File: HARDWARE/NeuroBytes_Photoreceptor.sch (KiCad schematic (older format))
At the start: 21 parts, among them P1 JST_GH_4-POS, P2 JST_GH_4-POS, P3 JST_GH_5-pos, SW1 SW_PB_4term, SW2 SW_PB_4term, U1 APDS9007, U2 STM32L011Gx, U3 3v3 LDO

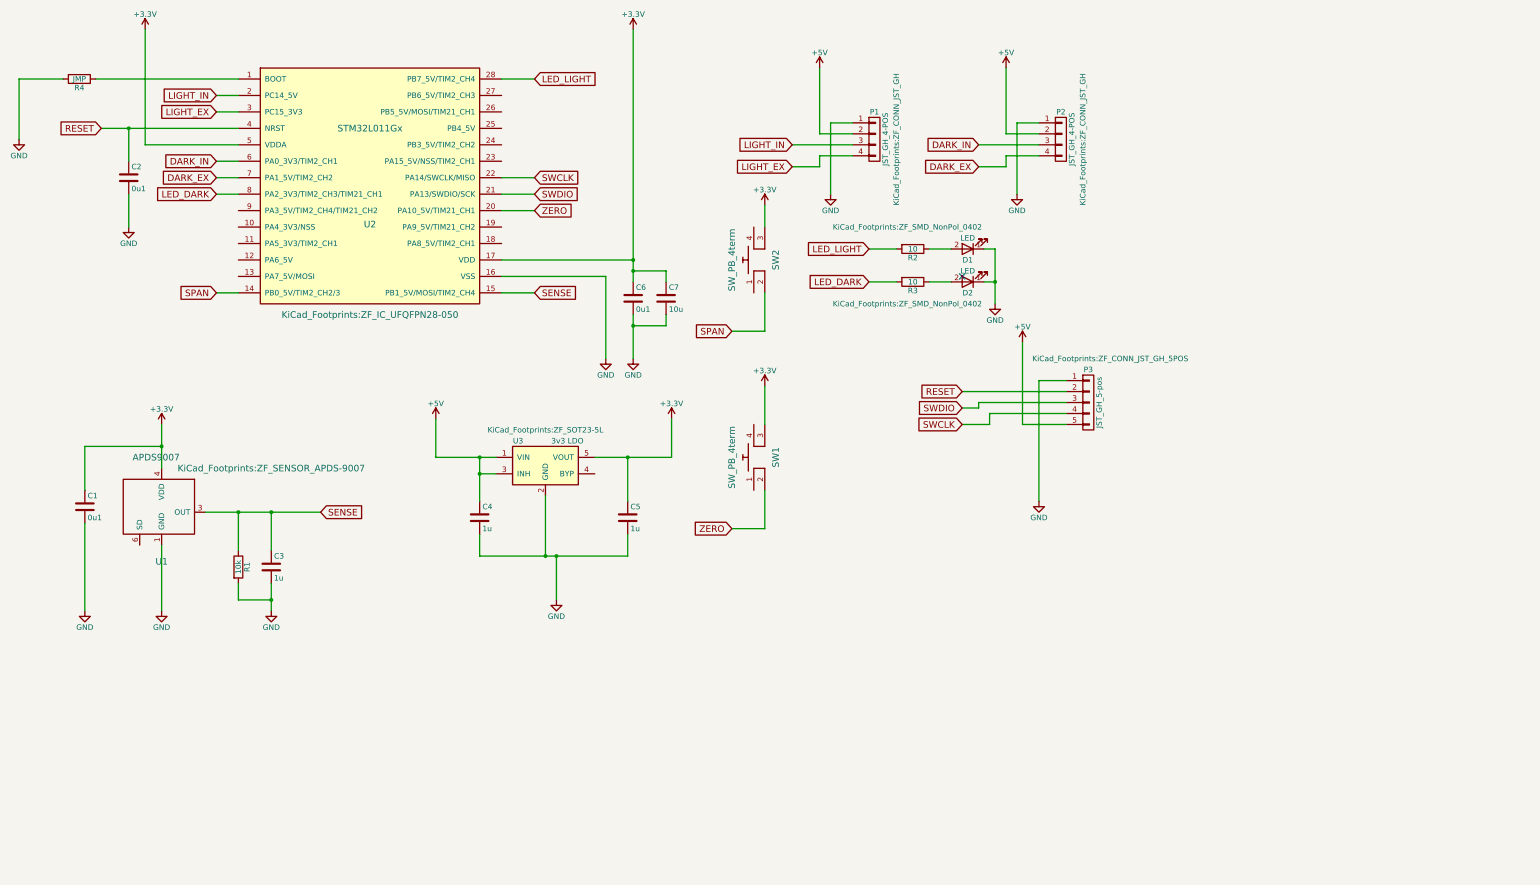
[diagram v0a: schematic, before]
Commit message: minor page layout updates
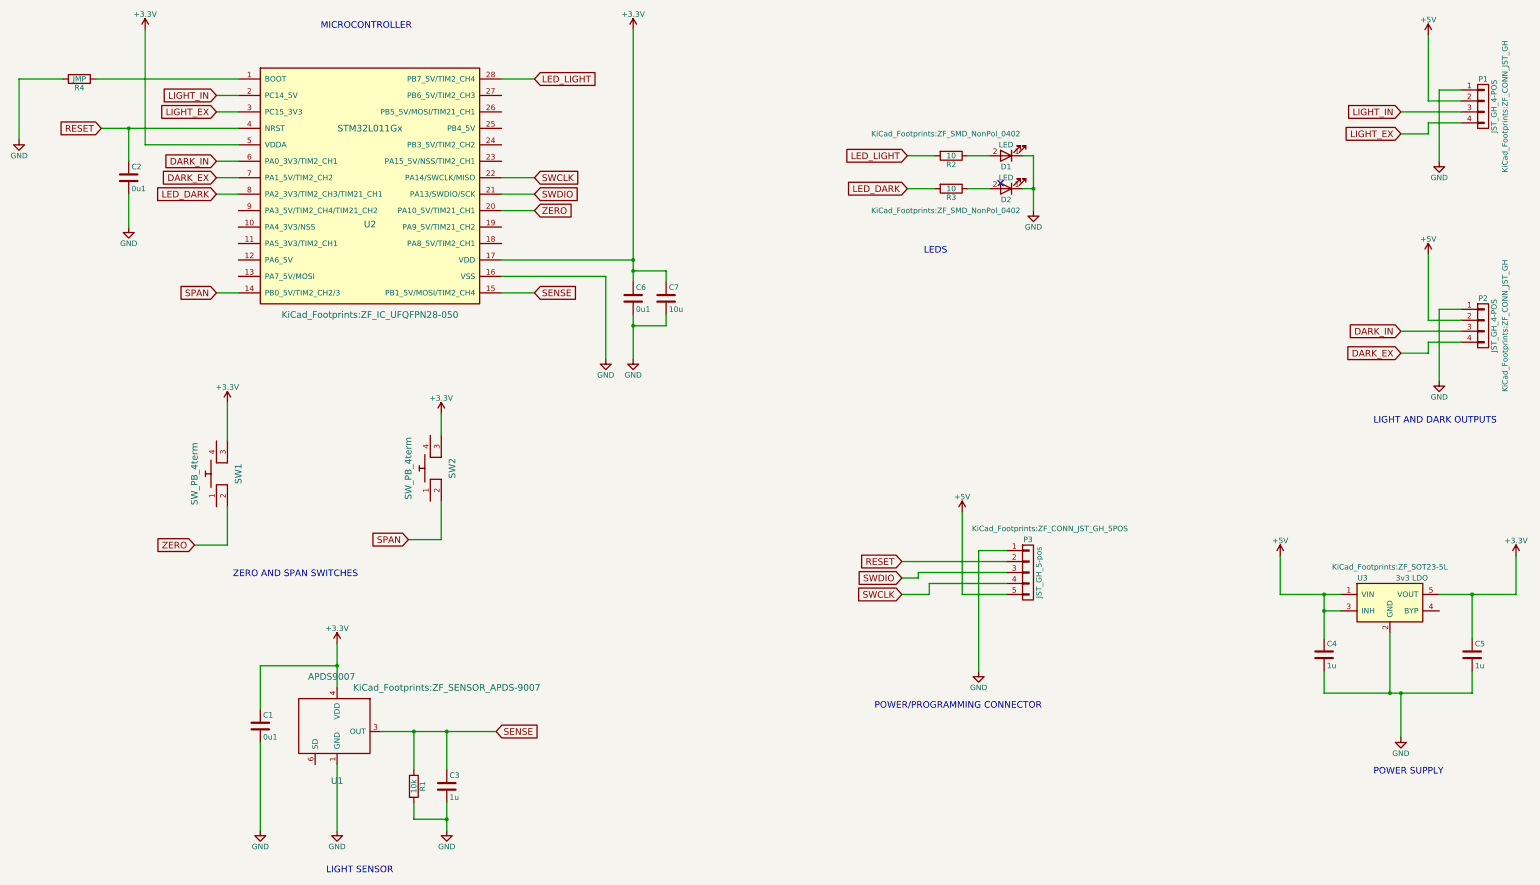
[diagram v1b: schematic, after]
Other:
- note added: "LEDS"
- note added: "LIGHT AND DARK OUTPUTS"
- note added: "LIGHT SENSOR"
- note added: "MICROCONTROLLER"
- note added: "POWER SUPPLY"
- note added: "POWER/PROGRAMMING CONNECTOR"
- note added: "ZERO AND SPAN SWITCHES"
- moved on the sheet: C1, C3, C4, C5, D1, D2, P1, P2, P3, R1, R2, R3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

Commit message: added ESD protection. updated title block. minor routing changes.
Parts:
- added U4: RClamp0503F, KiCad_Footprints:ZF_SMD_SOT-353, symbol RClamp0503F
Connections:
- net +3V3: now also U4.5 (VCC)
- net GND: now also U4.2 (GND)
- net SENSE: now also U4.1 (SIG1)
- net SPAN: now also U4.3 (SIG2)
- net ZERO: now also U4.4 (SIG3)
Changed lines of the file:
@@
 Rev "E"
 Comp "NeuroTinker LLC"
-Comment1 "License: GPL v3"
-Comment2 ""
+Comment1 "(C) 2018 Zach Fredin"
+Comment2 "License: CC-BY-SA 4.0"
 Comment3 ""
 Comment4 ""
@@
 $EndComp
 $Comp
-L +5V #PWR8
+L +5V #PWR01
 U 1 1 58B9AB7F
 P 12400 6100
-F 0 "#PWR8" H 12400 5950 50  0001 C CNN
+F 0 "#PWR01" H 12400 5950 50  0001 C CNN
 F 1 "+5V" H 12400 6240 50  0000 C CNN
 F 2 "" H 12400 6100 50  0000 C CNN
@@
 $EndComp
 $Comp
-L +3.3V #PWR13
+L +3.3V #PWR02
 U 1 1 58B9B0DC
 P 14550 6100
-F 0 "#PWR13" H 14550 5950 50  0001 C CNN
+F 0 "#PWR02" H 14550 5950 50  0001 C CNN
 F 1 "+3.3V" H 14550 6240 50  0000 C CNN
 F 2 "" H 14550 6100 50  0000 C CNN
@@
 $EndComp
 $Comp
-L GND #PWR9
+L GND #PWR03
 U 1 1 58B9B110
 P 13500 7750
-F 0 "#PWR9" H 13500 7500 50  0001 C CNN
+F 0 "#PWR03" H 13500 7500 50  0001 C CNN
 F 1 "GND" H 13500 7600 50  0000 C CNN
 F 2 "" H 13500 7750 50  0000 C CNN
@@
 $EndComp
 $Comp
-L +3.3V #PWR4
+L +3.3V #PWR04
 U 1 1 58B9B1C8
 P 2050 1300
-F 0 "#PWR4" H 2050 1150 50  0001 C CNN
+F 0 "#PWR04" H 2050 1150 50  0001 C CNN
 F 1 "+3.3V" H 2050 1440 50  0000 C CNN
 F 2 "" H 2050 1300 50  0000 C CNN
@@
 $EndComp
 $Comp
-L +3.3V #PWR11
+L +3.3V #PWR05
 U 1 1 58B9B218
 P 6500 1300
-F 0 "#PWR11" H 6500 1150 50  0001 C CNN
+F 0 "#PWR05" H 6500 1150 50  0001 C CNN
 F 1 "+3.3V" H 6500 1440 50  0000 C CNN
 F 2 "" H 6500 1300 50  0000 C CNN
@@
 $EndComp
 $Comp
-L GND #PWR10
+L GND #PWR06
 U 1 1 58B9B234
 P 6250 4300
-F 0 "#PWR10" H 6250 4050 50  0001 C CNN
+F 0 "#PWR06" H 6250 4050 50  0001 C CNN
 F 1 "GND" H 6250 4150 50  0000 C CNN
 F 2 "" H 6250 4300 50  0000 C CNN
@@
 $EndComp
 $Comp
-L GND #PWR3
+L GND #PWR07
 U 1 1 58B9B2B4
 P 1900 3100
-F 0 "#PWR3" H 1900 2850 50  0001 C CNN
+F 0 "#PWR07" H 1900 2850 50  0001 C CNN
 F 1 "GND" H 1900 2950 50  0000 C CNN
 F 2 "" H 1900 3100 50  0000 C CNN
@@
 	5600 2800 5300 2800
 $Comp
-L +5V #PWR21
+L +5V #PWR08
 U 1 1 58B9B77D
 P 9500 5700
-F 0 "#PWR21" H 9500 5550 50  0001 C CNN
+F 0 "#PWR08" H 9500 5550 50  0001 C CNN
 F 1 "+5V" H 9500 5840 50  0000 C CNN
 F 2 "" H 9500 5700 50  0000 C CNN
@@
 $EndComp
 $Comp
-L GND #PWR22
+L GND #PWR09
 U 1 1 58B9B796
 P 9650 7150
-F 0 "#PWR22" H 9650 6900 50  0001 C CNN
+F 0 "#PWR09" H 9650 6900 50  0001 C CNN
 F 1 "GND" H 9650 7000 50  0000 C CNN
 F 2 "" H 9650 7150 50  0000 C CNN
@@
 Connection ~ 6500 3400
 $Comp
-L GND #PWR12
+L GND #PWR010
 U 1 1 58B9C6F5
 P 6500 4300
-F 0 "#PWR12" H 6500 4050 50  0001 C CNN
+F 0 "#PWR010" H 6500 4050 50  0001 C CNN
 F 1 "GND" H 6500 4150 50  0000 C CNN
 F 2 "" H 6500 4300 50  0000 C CNN
@@
 	2050 2350 2900 2350
 $Comp
-L +5V #PWR19
+L +5V #PWR011
 U 1 1 58B9CBAC
 P 13750 3350
-F 0 "#PWR19" H 13750 3200 50  0001 C CNN
+F 0 "#PWR011" H 13750 3200 50  0001 C CNN
 F 1 "+5V" H 13750 3490 50  0000 C CNN
 F 2 "" H 13750 3350 50  0000 C CNN
@@
 	13750 3950 14050 3950
 $Comp
-L GND #PWR20
+L GND #PWR012
 U 1 1 58B9CC0C
 P 13850 4500
-F 0 "#PWR20" H 13850 4250 50  0001 C CNN
+F 0 "#PWR012" H 13850 4250 50  0001 C CNN
 F 1 "GND" H 13850 4350 50  0000 C CNN
 F 2 "" H 13850 4500 50  0000 C CNN
@@
 $EndComp
 $Comp
-L +5V #PWR16
+L +5V #PWR013
 U 1 1 58B9CEA4
 P 13750 1350
-F 0 "#PWR16" H 13750 1200 50  0001 C CNN
+F 0 "#PWR013" H 13750 1200 50  0001 C CNN
 F 1 "+5V" H 13750 1490 50  0000 C CNN
 F 2 "" H 13750 1350 50  0000 C CNN
@@
 	13750 1950 14050 1950
 $Comp
-L GND #PWR17
+L GND #PWR014
 U 1 1 58B9CEAC
 P 13850 2500
-F 0 "#PWR17" H 13850 2250 50  0001 C CNN
+F 0 "#PWR014" H 13850 2250 50  0001 C CNN
 F 1 "GND" H 13850 2350 50  0000 C CNN
 F 2 "" H 13850 2500 50  0000 C CNN
@@
 $EndComp
 $Comp
-L GND #PWR18
+L GND #PWR015
 U 1 1 58B9D2D7
 P 10150 2950
-F 0 "#PWR18" H 10150 2700 50  0001 C CNN
+F 0 "#PWR015" H 10150 2700 50  0001 C CNN
 F 1 "GND" H 10150 2800 50  0000 C CNN
 F 2 "" H 10150 2950 50  0000 C CNN
@@
 ZERO
 $Comp
-L +3.3V #PWR15
+L +3.3V #PWR016
 U 1 1 58B9D7AB
 P 2800 4700
-F 0 "#PWR15" H 2800 4550 50  0001 C CNN
+F 0 "#PWR016" H 2800 4550 50  0001 C CNN
 F 1 "+3.3V" H 2800 4840 50  0000 C CNN
 F 2 "" H 2800 4700 50  0000 C CNN
@@
 SPAN
 $Comp
-L +3.3V #PWR14
+L +3.3V #PWR017
 U 1 1 58B9D91D
 P 4750 4800
-F 0 "#PWR14" H 4750 4650 50  0001 C CNN
+F 0 "#PWR017" H 4750 4650 50  0001 C CNN
 F 1 "+3.3V" H 4750 4940 50  0000 C CNN
 F 2 "" H 4750 4800 50  0000 C CNN
@@
 $EndComp
 $Comp
-L +3.3V #PWR5
+L +3.3V #PWR018
 U 1 1 58B9DDBA
 P 3800 6900
-F 0 "#PWR5" H 3800 6750 50  0001 C CNN
+F 0 "#PWR018" H 3800 6750 50  0001 C CNN
 F 1 "+3.3V" H 3800 7040 50  0000 C CNN
 F 2 "" H 3800 6900 50  0000 C CNN
@@
 	3800 6900 3800 7300
 $Comp
-L GND #PWR6
+L GND #PWR019
 U 1 1 58B9DE4B
 P 3800 8600
-F 0 "#PWR6" H 3800 8350 50  0001 C CNN
+F 0 "#PWR019" H 3800 8350 50  0001 C CNN
 F 1 "GND" H 3800 8450 50  0000 C CNN
 F 2 "" H 3800 8600 50  0000 C CNN
@@
 $EndComp
 $Comp
-L GND #PWR7
+L GND #PWR020
 U 1 1 58B9DF7E
 P 4800 8600
-F 0 "#PWR7" H 4800 8350 50  0001 C CNN
+F 0 "#PWR020" H 4800 8350 50  0001 C CNN
 F 1 "GND" H 4800 8450 50  0000 C CNN
 F 2 "" H 4800 8600 50  0000 C CNN
@@
 Connection ~ 3800 7100
 $Comp
-L GND #PWR2
+L GND #PWR021
 U 1 1 58B9E313
 P 3100 8600
-F 0 "#PWR2" H 3100 8350 50  0001 C CNN
+F 0 "#PWR021" H 3100 8350 50  0001 C CNN
 F 1 "GND" H 3100 8450 50  0000 C CNN
 F 2 "" H 3100 8600 50  0000 C CNN
@@
 $EndComp
 $Comp
-L GND #PWR1
+L GND #PWR022
 U 1 1 590B4A9C
 P 900 2300
-F 0 "#PWR1" H 900 2050 50  0001 C CNN
+F 0 "#PWR022" H 900 2050 50  0001 C CNN
 F 1 "GND" H 900 2150 50  0000 C CNN
 F 2 "" H 900 2300 50  0000 C CNN
@@
 Text Notes 13250 4900 0    60   ~ 0
 LIGHT AND DARK OUTPUTS
+$Comp
+L RClamp0503F U4
+U 1 1 5A835A02
+P 7050 5600
+F 0 "U4" H 7050 5200 60  0000 C CNN
+F 1 "RClamp0503F" H 7050 6000 60  0000 C CNN
+F 2 "KiCad_Footprints:ZF_SMD_SOT-353" H 7200 5450 60  0001 C CNN
+F 3 "" H 7200 5450 60  0001 C CNN
+F 4 "No" H 7050 5600 60  0001 C CNN "Subs Allowed"
+F 5 "Yes" H 7050 5600 60  0001 C CNN "RoHS"
+	1    7050 5600
+	1    0    0    -1
+$EndComp
+$Comp
+L GND #PWR023
+U 1 1 5A835AC3
+P 6350 6350
+F 0 "#PWR023" H 6350 6100 50  0001 C CNN
+F 1 "GND" H 6350 6200 50  0000 C CNN
+F 2 "" H 6350 6350 50  0001 C CNN
+F 3 "" H 6350 6350 50  0001 C CNN
+	1    6350 6350
+	1    0    0    -1
+$EndComp
+Wire Wire Line
+	6350 6350 6350 5600
+Wire Wire Line
+	6350 5600 6600 5600
+Text GLabel 6150 5800 0    60   Input ~ 0
+SPAN
+Wire Wire Line
+	6150 5400 6600 5400
+Text GLabel 7850 5800 2    60   Input ~ 0
+ZERO
+Wire Wire Line
+	6150 5800 6600 5800
+$Comp
+L +3.3V #PWR024
+U 1 1 5A835D13
+P 7750 5050
+F 0 "#PWR024" H 7750 4900 50  0001 C CNN
+F 1 "+3.3V" H 7750 5190 50  0000 C CNN
+F 2 "" H 7750 5050 50  0001 C CNN
+F 3 "" H 7750 5050 50  0001 C CNN
+	1    7750 5050
+	1    0    0    -1
+$EndComp
+Wire Wire Line
+	7750 5050 7750 5400
+Wire Wire Line
+	7750 5400 7500 5400
+Text GLabel 6150 5400 0    60   Input ~ 0
+SENSE
+Wire Wire Line
+	7850 5800 7500 5800
 $EndSCHEMATC

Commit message: generated fab files. generated BOM.
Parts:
- U4: Link (none) -> https://www.digikey.com/product-detail/en/semtech-corporati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; Mfr (none) -> Semtech Corporation; Mfr Part # (none) -> RCLAMP0503F.TCT; Package (none) -> 5-TSSOP
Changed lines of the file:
@@
 F 2 "KiCad_Footprints:ZF_SMD_SOT-353" H 7200 5450 60  0001 C CNN
 F 3 "" H 7200 5450 60  0001 C CNN
-F 4 "No" H 7050 5600 60  0001 C CNN "Subs Allowed"
-F 5 "Yes" H 7050 5600 60  0001 C CNN "RoHS"
+F 4 "Semtech Corporation" H 7050 5600 60  0001 C CNN "Mfr"
+F 5 "RCLAMP0503F.TCT" H 7050 5600 60  0001 C CNN "Mfr Part #"
+F 6 "5-TSSOP" H 7050 5600 60  0001 C CNN "Package"
+F 7 "https://www.digikey.com/product-detail/en/semtech-corporation/RCLAMP0503F.TCT/RCLAMP0503F.TCTTR-ND/5113629" H 7050 5600 60  0001 C CNN "Link"
+F 8 "No" H 7050 5600 60  0001 C CNN "Subs Allowed"
+F 9 "Yes" H 7050 5600 60  0001 C CNN "RoHS"
 	1    7050 5600
 	1    0    0    -1

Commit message: updated footprints to include B.Fab outlines. minor routing changes. re-generated Gerbers. added placement pdf.
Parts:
- C3, C4, C5: footprint KiCad_Footprints:ZF_SMD_NonPol_0603 -> Capacitors_SMD:C_0603_HandSoldering
- C7: footprint KiCad_Footprints:ZF_SMD_nonpol_1206 -> Capacitors_SMD:C_1206
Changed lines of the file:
@@
 F 0 "C4" H 12825 7100 50  0000 L CNN
 F 1 "1u" H 12825 6900 50  0000 L CNN
-F 2 "KiCad_Footprints:ZF_SMD_NonPol_0603" H 12838 6850 50  0001 C CNN
+F 2 "Capacitors_SMD:C_0603_HandSoldering" H 12838 6850 50  0001 C CNN
 F 3 "" H 12800 7000 50  0000 C CNN
 F 4 "Taiyo Yuden" H 12800 7000 60  0001 C CNN "Mfr"
@@
 F 0 "C7" H 6825 3850 50  0000 L CNN
 F 1 "10u" H 6825 3650 50  0000 L CNN
-F 2 "KiCad_Footprints:ZF_SMD_nonpol_1206" H 6838 3600 50  0001 C CNN
+F 2 "Capacitors_SMD:C_1206" H 6838 3600 50  0001 C CNN
 F 3 "" H 6800 3750 50  0000 C CNN
 F 4 "Taiyo Yuden" H 6800 3750 60  0001 C CNN "Mfr"
@@
 F 0 "C5" H 14175 7100 50  0000 L CNN
 F 1 "1u" H 14175 6900 50  0000 L CNN
-F 2 "KiCad_Footprints:ZF_SMD_NonPol_0603" H 14188 6850 50  0001 C CNN
+F 2 "Capacitors_SMD:C_0603_HandSoldering" H 14188 6850 50  0001 C CNN
 F 3 "" H 14150 7000 50  0000 C CNN
 F 4 "Taiyo Yuden" H 14150 7000 60  0001 C CNN "Mfr"
@@
 F 0 "C3" H 4825 8300 50  0000 L CNN
 F 1 "1u" H 4825 8100 50  0000 L CNN
-F 2 "KiCad_Footprints:ZF_SMD_NonPol_0603" H 4838 8050 50  0001 C CNN
+F 2 "Capacitors_SMD:C_0603_HandSoldering" H 4838 8050 50  0001 C CNN
 F 3 "" H 4800 8200 50  0000 C CNN
 F 4 "Taiyo Yuden" H 4800 8200 60  0001 C CNN "Mfr"
